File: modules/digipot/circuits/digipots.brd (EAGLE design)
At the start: 72.1 x 38.1 mm, 13 parts

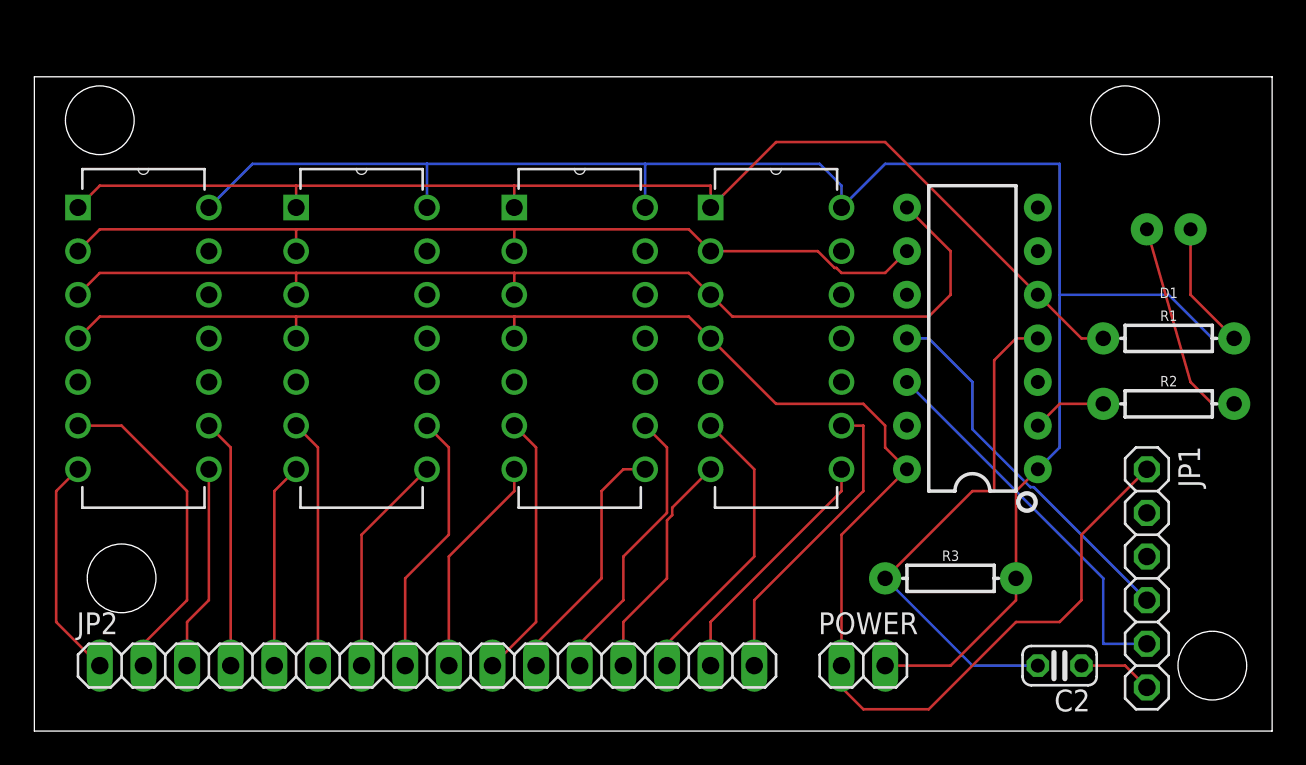
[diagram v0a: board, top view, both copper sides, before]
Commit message: digipots CV
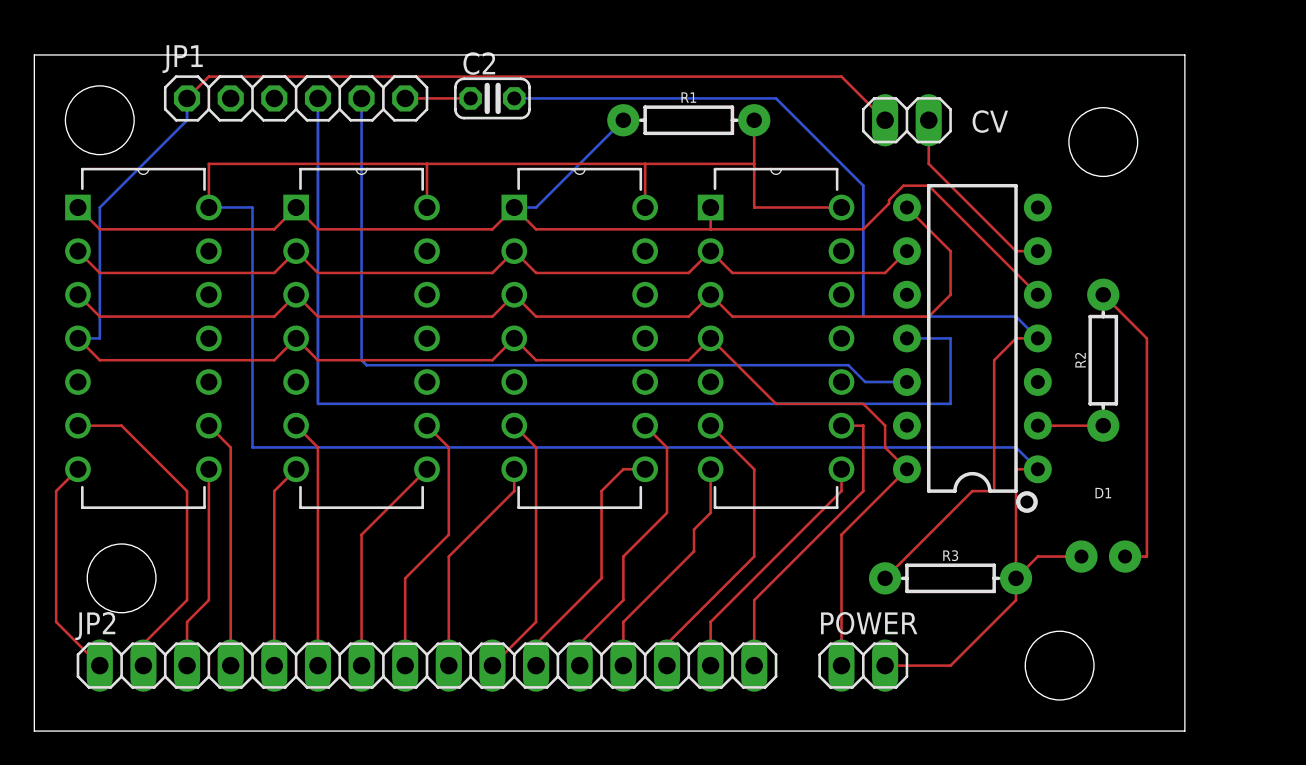
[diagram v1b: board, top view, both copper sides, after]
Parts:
- added CV: (no value), pinhead:1X02
- moved JP1 56.9 mm to (15.2, 36.8), turned to 0 degrees
- moved C2 46.7 mm to (26.7, 36.8), turned to 0 degrees
- moved R1 30.7 mm to (38.1, 35.6)
- moved D1 19.4 mm to (62.2, 10.2), turned to 0 degrees
- moved R2 4.58 mm to (62.2, 21.6), turned to 90 degrees
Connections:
- new net N$26: ATTINY44.6, CV.2
- net GND: now also CV.1
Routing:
- net N$25: track 21.9 -> 61.0 mm
- net GND: track 96.4 -> 129.2 mm
- net N$22: track 30.1 -> 59.9 mm
- net N$23: track 22.5 -> 47.5 mm
- net 5V: track 112.8 -> 134.7 mm
- net N$26: track 0.00 -> 11.0 mm
- net N$21: track 12.3 -> 17.6 mm
- net N$17: track 70.3 -> 72.0 mm
- net N$19: track 4.34 -> 3.81 mm
- net N$24: track 4.34 -> 3.81 mm
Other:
- board size 72.1 x 38.1 mm -> 67 x 39.4 mm
- board text added: "CV to 8 resistances converter"
